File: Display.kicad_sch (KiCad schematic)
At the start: 10 parts, among them J2 TFT_LCD, J3 CAPACITIVE_CONTROLLER

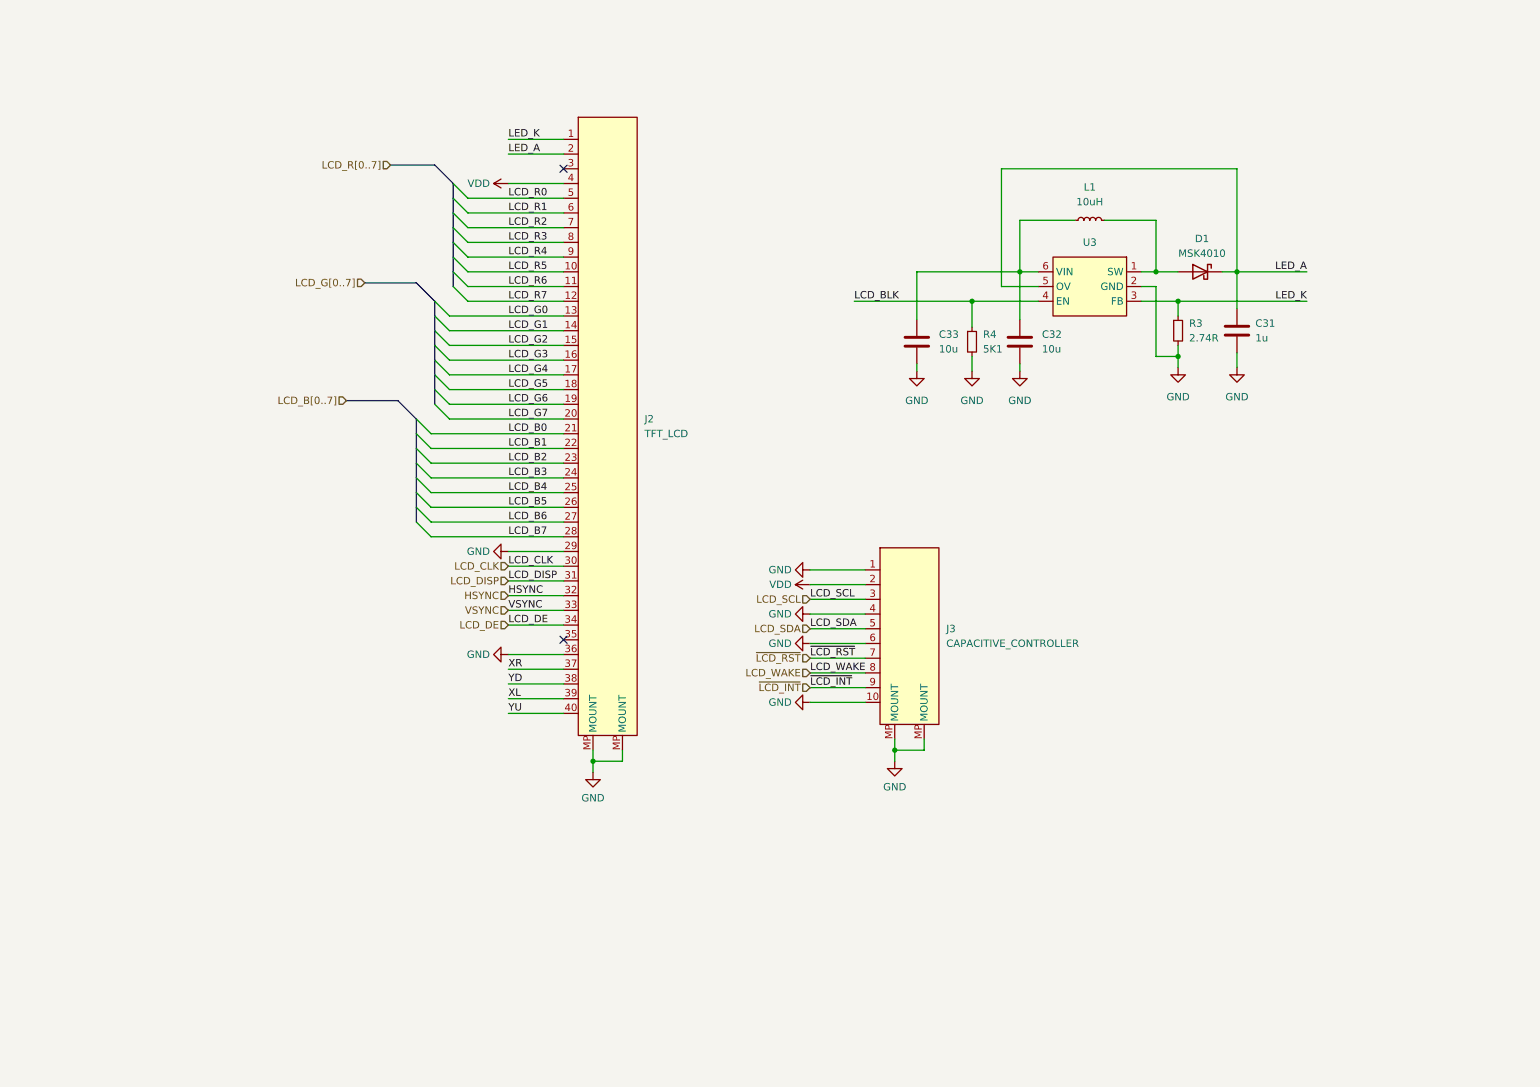
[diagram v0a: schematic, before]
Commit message: Added UART, i2c, debug, NAND Flash, NOR Flash, EEPROM, SD-Card
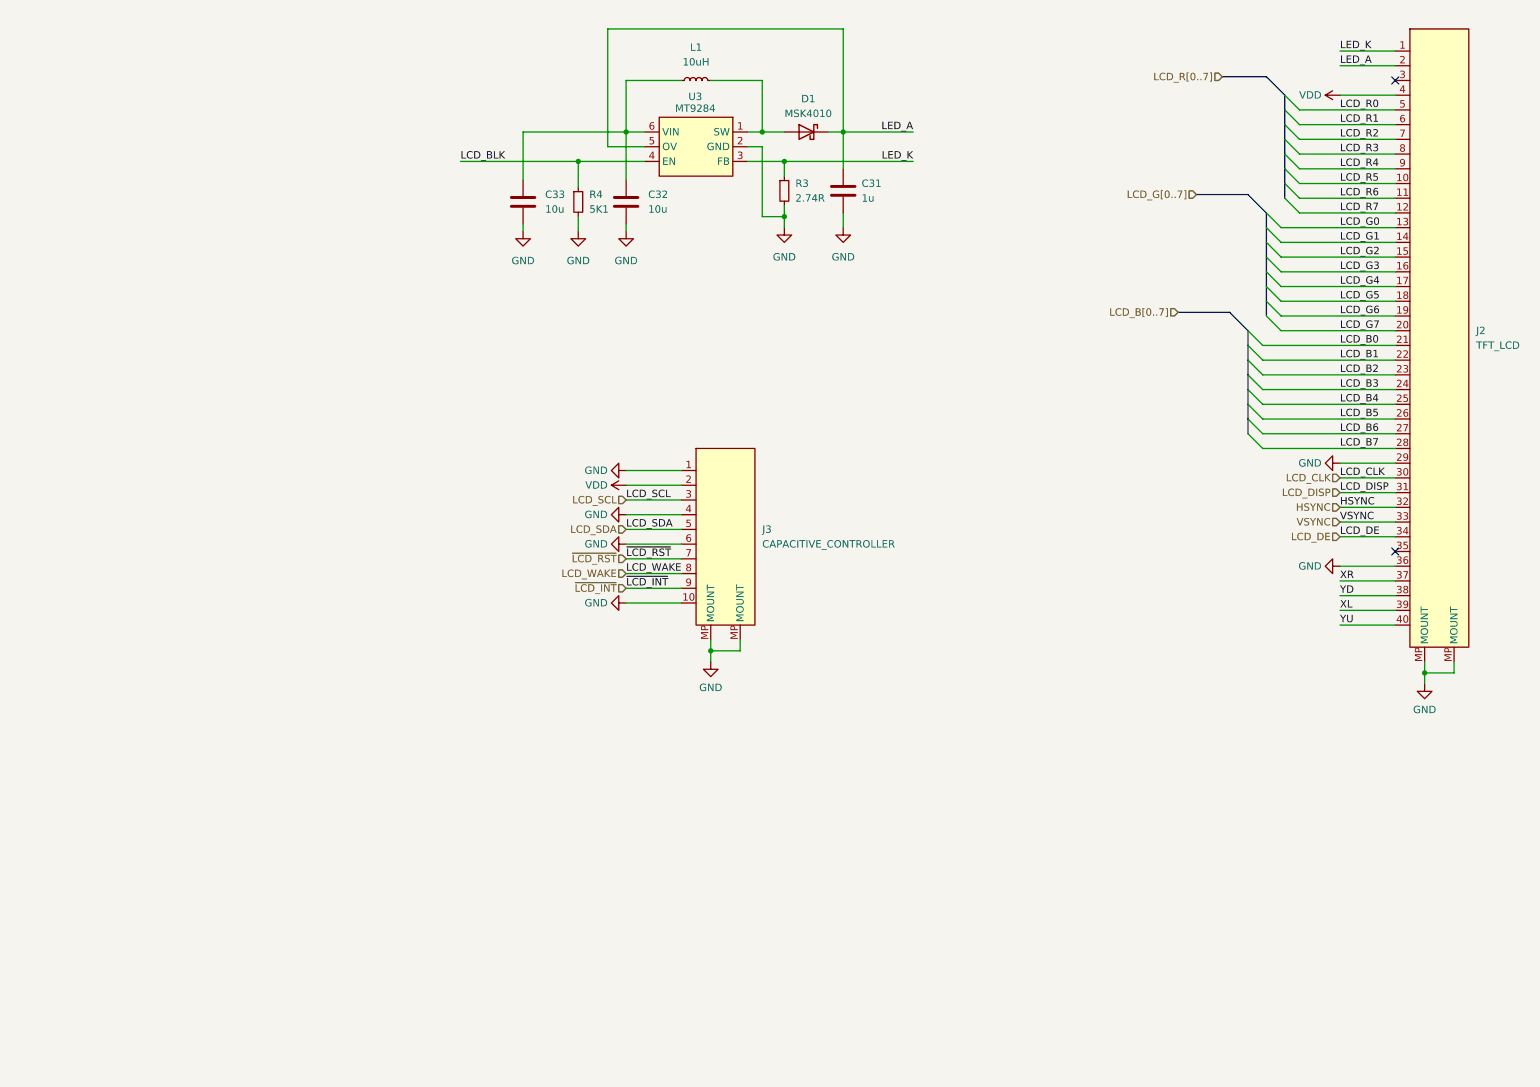
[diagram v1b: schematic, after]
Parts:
- C31, C32, C33: footprint (none) -> Capacitor_SMD:C_0603_1608Metric
- D1: footprint (none) -> Diode_SMD:D_SOD-123
- L1: footprint (none) -> Inductor_SMD:L_1210_3225Metric
- R3, R4: footprint (none) -> Resistor_SMD:R_0402_1005Metric
- U3: value ~ -> MT9284; footprint (none) -> Package_TO_SOT_SMD:SOT-23-6
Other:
- moved on the sheet: C31, C32, C33, D1, J2, J3, L1, R3, R4, U3

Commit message: Added I2S Audio amplifier
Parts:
- D1: footprint Diode_SMD:D_SOD-123 -> Diode_SMD:D_SOD-523
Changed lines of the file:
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@@
 			)
 		)
-		(property "Footprint" "Diode_SMD:D_SOD-123"
+		(property "Footprint" "Diode_SMD:D_SOD-523"
 			(at 148.59 41.91 0)
 			(effects

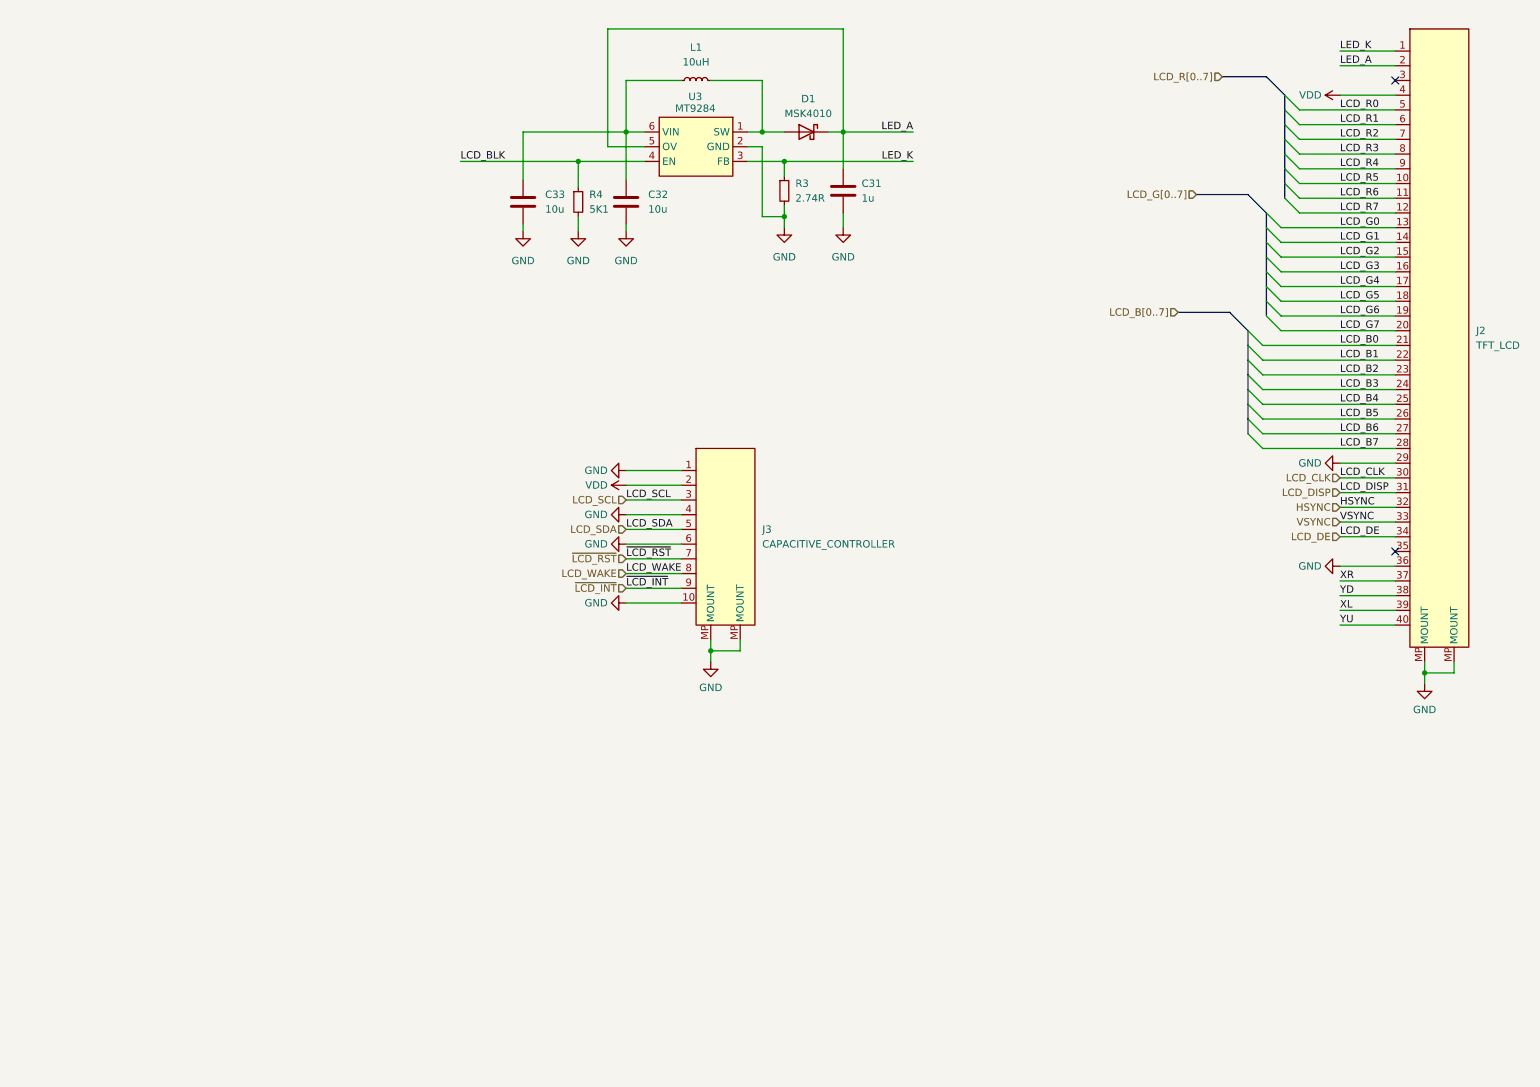
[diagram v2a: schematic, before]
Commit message: Finish sdram, LCD, SD-card, QSPI, I2S tracks
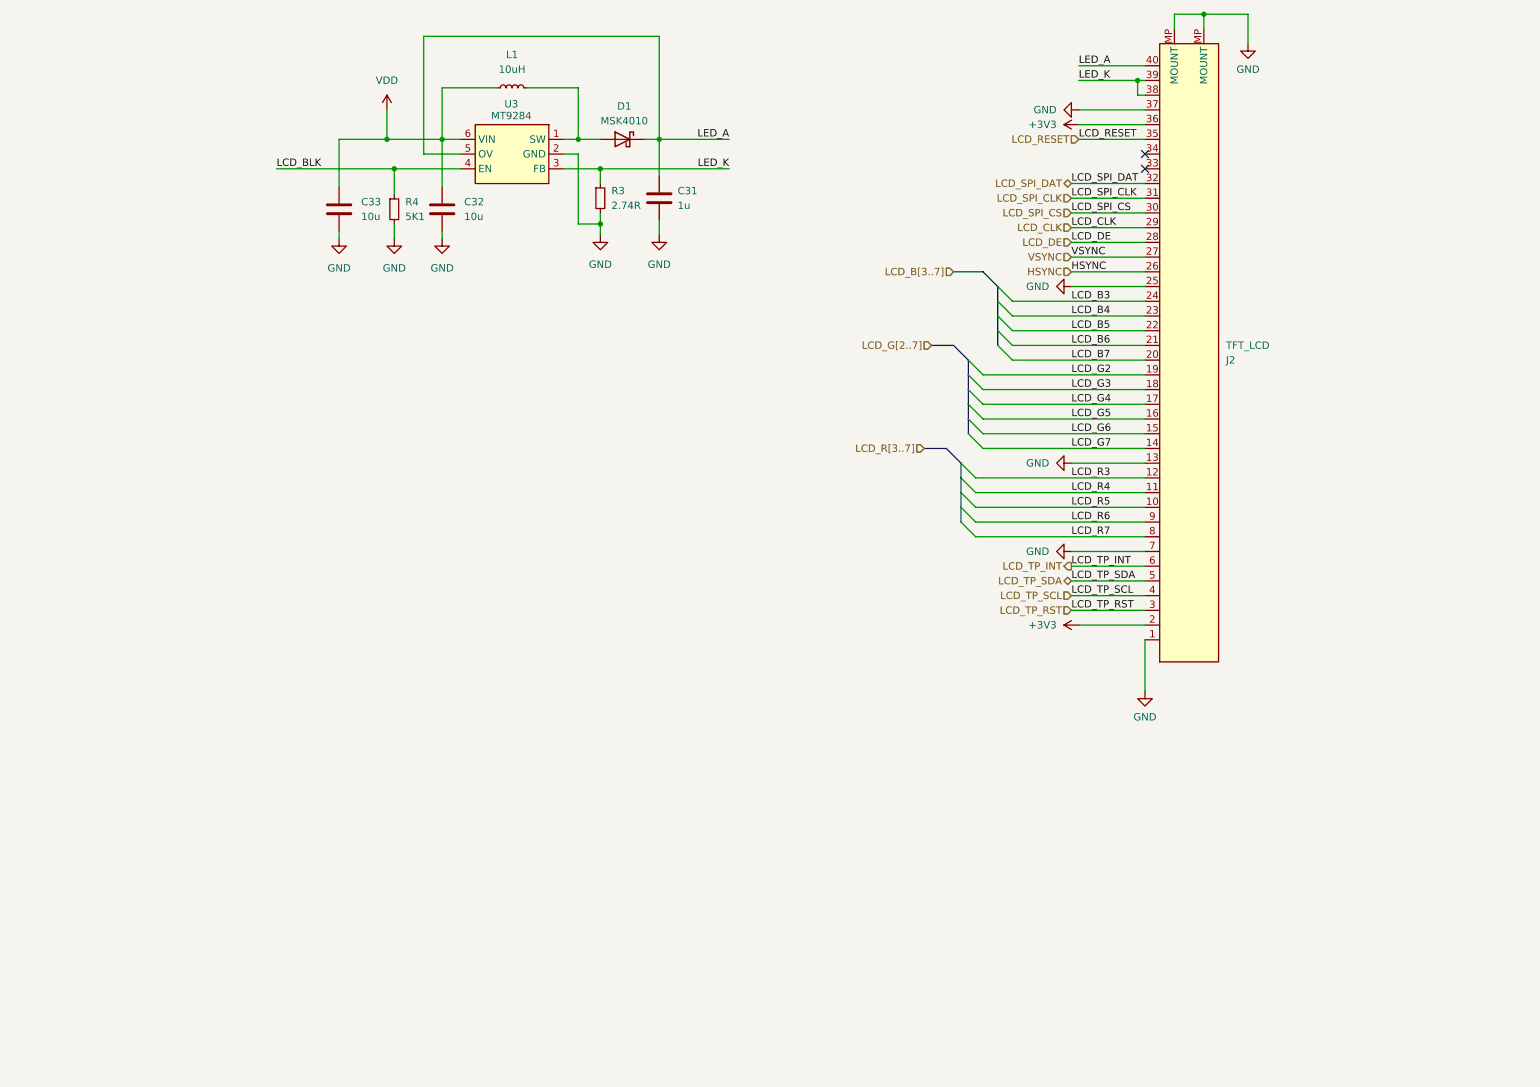
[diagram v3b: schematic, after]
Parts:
- removed J3: CAPACITIVE_CONTROLLER, Connector_FFC-FPC:Hirose_FH12-10S-0.5SH_1x10-1MP_P0.50mm_Horizontal, symbol FPC_10P_double_contact:FPC-10P
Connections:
- net LCD_B0 is gone; now on net LCD_B6: J2.21
- net LCD_B1 is gone; now on net LCD_B5: J2.22
- net LCD_B2 is gone; now on net LCD_B4: J2.23
- net LCD_G0 is gone; now on net GND: J2.13
- net LCD_G1 is gone; now on net LCD_G7: J2.14
- net LCD_R2 is gone; now on net GND: J2.7
- net XL is gone; now on net LED_K: J2.39
- net XR is gone; now on net GND: J2.37
- net YD is gone; now on net LED_K: J2.38
- net YU is gone; now on net LED_A: J2.40
- net GND: now also J2.1, J2.25; no longer J2.29, J2.36
- net HSYNC: now also J2.26; no longer J2.32
- net LCD_B4: no longer J2.25
- net LCD_B5: no longer J2.26
- net LCD_B6: no longer J2.27
- net LCD_B7: now also J2.20; no longer J2.28
- net LCD_CLK: now also J2.29; no longer J2.30
- net LCD_DE: now also J2.28; no longer J2.34
- net LCD_G2: now also J2.19; no longer J2.15
- net LCD_G3: now also J2.18; no longer J2.16
- net LCD_G5: now also J2.16; no longer J2.18
- net LCD_G6: now also J2.15; no longer J2.19
- net LCD_G7: no longer J2.20
- net LCD_R3: now also J2.12; no longer J2.8
- net LCD_R4: now also J2.11; no longer J2.9
- net LCD_R6: now also J2.9; no longer J2.11
- net LCD_R7: now also J2.8; no longer J2.12
- net LED_A: no longer J2.2
- net LED_K: no longer J2.1
- net VDD: now also C32.1, C33.1, L1.1, U3.6 (VIN); no longer J2.4
- net VSYNC: now also J2.27; no longer J2.33
- net LCD_TP_RST: now reaches J2.3
- net LCD_RESET: now reaches J2.35
- net LCD_DISP renamed LCD_SPI_CLK
- net LCD_R0 renamed LCD_TP_SDA
- net LCD_R1 renamed LCD_TP_INT
- new net +3V3: J2.2, J2.36
- new net LCD_SPI_CS: J2.30
- new net LCD_SPI_DAT: J2.32
- new net LCD_TP_SCL: J2.4
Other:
- moved on the sheet: C31, C32, C33, D1, J2, L1, R3, R4, U3
